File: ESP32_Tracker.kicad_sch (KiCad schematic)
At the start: 0 parts

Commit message: initial schematic started
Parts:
- added C1, C6: 0.1u, symbol Device:C
- added C2: 22u, symbol Device:C
- added C3: 1u, symbol Device:C
- added C4, C5: 10u, symbol Device:C
- added H1, H2, H3, H4: MountingHole_Pad, symbol Mechanical:MountingHole_Pad
- added J1: USB_C_Receptacle_USB2.0_16P, symbol Connector:USB_C_Receptacle_USB2.0_16P
- added R1, R2: 10k, symbol Device:R_US
- added R3, R4: 2.2k, symbol Device:R_US
- added R5, R6: 5.1k, symbol Device:R_US
- added SW1, SW2: SW_Push, symbol Switch:SW_Push
- added TP1, TP2, TP3, TP4: TestPoint, symbol Connector:TestPoint
- added U1: ESP32-S3-MINI-1, RF_Module:ESP32-S2-MINI-1, symbol RF_Module:ESP32-S3-MINI-1
- added U2: USBLC6-2SC6, Package_TO_SOT_SMD:SOT-23-6, symbol Power_Protection:USBLC6-2SC6
- added U3: XC6220B331MR-G, Package_TO_SOT_SMD:SOT-23-5, symbol Regulator_Linear:XC6220B331MR
- added U4: SAM-M10Q, RF_GPS:ublox_SAM-M8Q, symbol RF_GPS:SAM-M8Q
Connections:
- new net: J1.A5 (CC1), R5.2
- new net: J1.A6 (D+), J1.B6 (D+), U2.3 (I/O2)
- new net: J1.A7 (D-), J1.B7 (D-), U2.1 (I/O1)
- new net: J1.B5 (CC2), R6.1
- new net: R1.1, SW2.1, TP4.1, U1.4 (IO0)
- new net: C3.1, R2.1, SW1.2, TP3.1, U1.45 (EN)
- new net +3.3V: C1.1, C2.1, C5.1, C6.1, R1.2, R2.2, R3.2, R4.2, TP2.1, U1.3 (3V3), U3.5 (VOUT), U4.17 (VCC), U4.2 (VCC_IO)
- new net GND: C1.2, C2.2, C3.2, C4.1, C5.2, C6.2, J1.A1 (GND), J1.A12 (GND), J1.B1 (GND), J1.B12 (GND), J1.S1 (SHIELD), R5.1, R6.2, SW1.1, SW2.2, U1.1 (GND), U1.2 (GND), U1.42 (GND), U1.43 (GND), U1.46 (GND), U1.47 (GND), U1.48 (GND), U1.49 (GND), U1.50 (GND), U1.51 (GND), U1.52 (GND), U1.53 (GND), U1.54 (GND), U1.55 (GND), U1.56 (GND), U1.57 (GND), U1.58 (GND), U1.59 (GND), U1.60 (GND), U1.61 (GND), U1.62 (GND), U1.63 (GND), U1.64 (GND), U1.65 (GND), U2.2 (GND), U3.2 (GND), U4.1 (GND), U4.10 (GND), U4.11 (GND), U4.15 (GND), U4.16 (GND), U4.20 (GND), U4.4 (GND), U4.5 (GND), U4.6 (GND)
- new net GPS_CLK: R3.1, U1.15 (IO11), U4.12 (SCL)
- new net GPS_DATA: R4.1, U1.14 (IO10), U4.9 (SDA)
- new net USB_N: U1.23 (USB_D-), U2.6 (I/O1)
- new net USB_P: U1.24 (USB_D+), U2.4 (I/O2)
- new net VBUS: C4.2, J1.A4 (VBUS), J1.A9 (VBUS), J1.B4 (VBUS), J1.B9 (VBUS), TP1.1, U2.5 (VBUS), U3.1 (VIN), U3.3 (CE)
- no-connect marks 0 -> 8
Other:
- note added: "(4.5, 5, 5.5)V"
- note added: "5v -> 3.3v @ 1A 60mV @ 300mA"
- note added: "BOOT"
- note added: "RESET"
- note added: "Reset button? clears GNSS data and config stored in BBR"
- note added: "USB-C (DONE) LDO (DONE) GPS (IN PROGRESS) MAGNETOMETER MICROSD BATTERY MGMT."
- note added: "bypass caps typ. app."
- note added: "have primary LiPo act as backup? or add small coincell?"
- note added: "timepulse LED?"
- note added: "typ. app."
- title: (none) -> ESP32 Telemetry Tracker Board

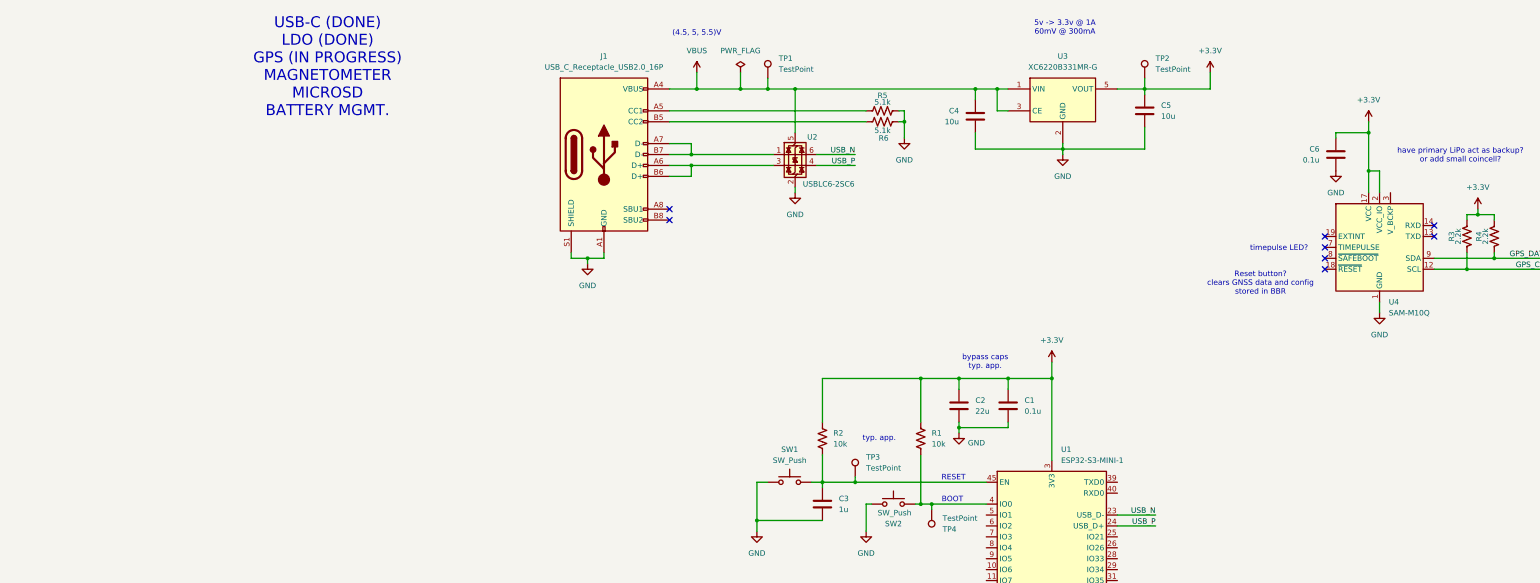
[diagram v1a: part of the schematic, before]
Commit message: magnt. symbol created
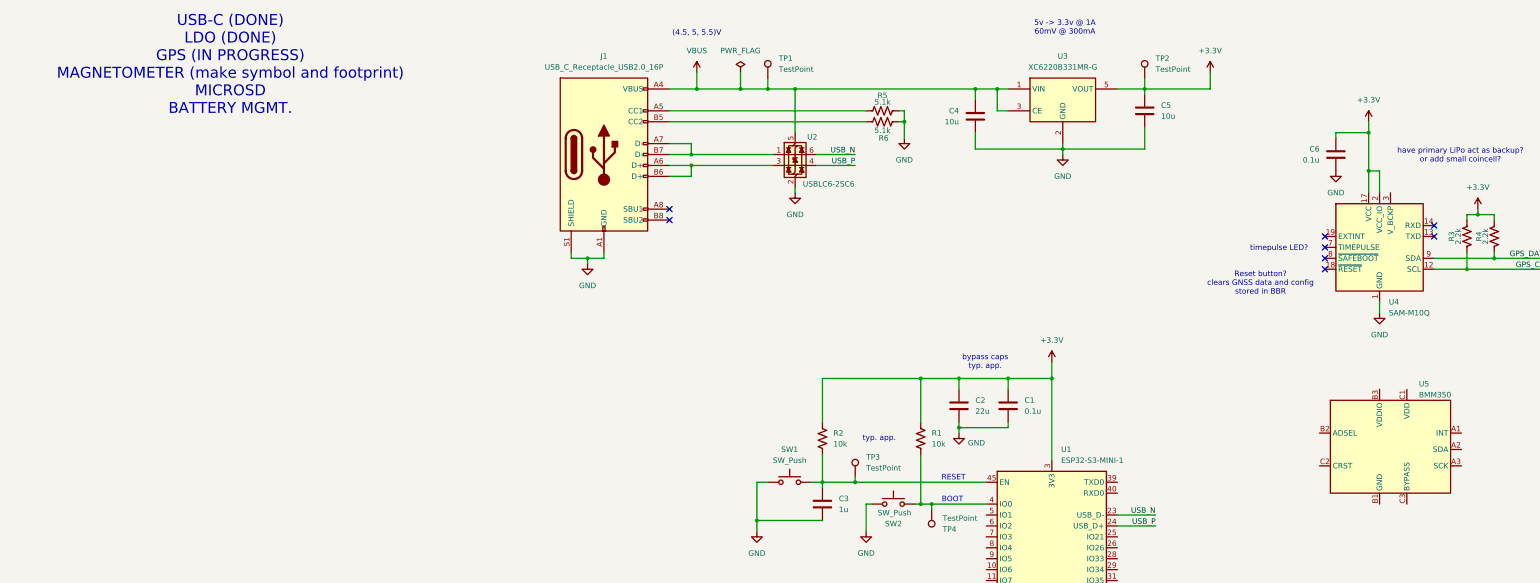
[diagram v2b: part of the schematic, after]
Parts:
- added U5: BMM350, symbol BMM350:BMM350
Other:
- note added: "USB-C (DONE) LDO (DONE) GPS (IN PROGRESS) MAGNETOMETER (make symbol and footprint) MICROSD BATTERY MGMT."
- note removed: "USB-C (DONE) LDO (DONE) GPS (IN PROGRESS) MAGNETOMETER MICROSD BATTERY MGMT."
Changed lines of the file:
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@@
 		)
 	)
-	(text "USB-C (DONE)\nLDO (DONE)\nGPS (IN PROGRESS)\nMAGNETOMETER\nMICROSD\nBATTERY MGMT."
+	(text "USB-C (DONE)\nLDO (DONE)\nGPS (IN PROGRESS)\nMAGNETOMETER (make symbol and footprint)\nMICROSD\nBATTERY MGMT."
 		(exclude_from_sim no)
-		(at -27.432 27.94 0)
+		(at -50.038 27.432 0)
 		(effects
 			(font
@@
 					(unit 1)
 				)
+			)
+		)
+	)
+	(symbol
+		(lib_id "BMM350:BMM350")
+		(at 219.71 115.57 0)
+		(unit 1)
+		(exclude_from_sim no)
+		(in_bom yes)
+		(on_board yes)
+		(dnp no)
+		(property "Reference" "U5"
+			(at 226.314 101.6 0)
+			(effects
+				(font
+					(size 1.27 1.27)
+				)
+				(justify left)
+			)
+		)
+		(property "Value" "BMM350"
+			(at 226.314 104.14 0)
+			(effects
+				(font
+					(size 1.27 1.27)
+				)
+				(justify left)
+			)
+		)
+		(property "Footprint" ""
+			(at 219.71 115.57 0)
+			(effects
+				(font
+					(size 1.27 1.27)
+				)
+				(hide yes)
+			)
+		)
+		(property "Datasheet" ""
+			(at 219.71 115.57 0)
+			(effects
+				(font
+					(size 1.27 1.27)
+				)
+				(hide yes)
+			)
+		)
+		(property "Description" ""
+			(at 219.71 115.57 0)
+			(effects
+				(font
+					(size 1.27 1.27)
+				)
+				(hide yes)
+			)
+		)
+		(pin "C1"
+		)
+		(pin "B2"
+		)
+		(pin "C2"
+		)
+		(pin "B3"
+		)
+		(pin "B1"
+		)
+		(pin "A1"
+		)
+		(pin "A2"
+		)
+		(pin "C3"
+		)
+		(pin "A3"
+		)
+		(instances
+			(project ""
+				(path "/92195c42-0bc4-473e-a890-6f85786d3c69"
+					(reference "U5")
+					(unit 1)
+				)

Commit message: new magnetometer
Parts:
- removed U5: BMM350, symbol BMM350:BMM350
- added C10, C11, C8, C9: 0.1u, symbol Device:C
- added C12: 10u, symbol Device:C
- added C13: 0.22u, symbol Device:C
- added C7: 2.2u, symbol Device:C
- added R7, R8: 10k, symbol Device:R_US
- added U5: BMM350, Package_BGA_Custom:WLCSP-9_1.28x1.28mm_P0.4mm_Bosch_BMM350, symbol Sensor_Magnetometer_Bosch:BMM350
- added U6: LIS2MDL, Package_LGA:LGA-12_2x2mm_P0.5mm, symbol Sensor_Magnetic:LIS2MDL
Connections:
- net +3.3V: now also C10.1, C11.1, C12.1, C8.1, C9.1, R7.2, R8.2, U5.B3 (VDDIO), U5.C1 (VDD), U6.10 (Vdd_IO), U6.3 (~{CS}), U6.9 (Vdd)
- net GND: now also C10.2, C11.2, C12.2, C13.2, C7.1, C8.2, C9.2, U5.B1 (GND), U5.B2 (ADSEL), U5.C3 (BYPASS), U6.6 (GND), U6.8 (GND)
- net MAG_DATA: now reaches U1.18 (IO14)
- net MAG_DATA: now also R8.1, U6.4 (SDA/SDI/SDO)
- net MAG_CLK: now reaches U1.19 (IO15)
- net MAG_CLK: now also R7.1, U6.1 (SCL/SPC)
- net MAG_INT: now reaches U1.20 (IO16)
- net MAG_INT: now also U6.7 (DRDY)
- new net: C13.1, U6.5 (C1)
- new net: C7.2, U5.C2 (CRST)
- no-connect marks 8 -> 39
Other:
- note added: "B3/C1 both need 0.1uF bypass cap TYP.APP."
- note added: "HIGH for I2C"
- note added: "LOW = 0x14 TYP.APP."
- note added: "USB-C (DONE) LDO (DONE) GPS (IN PROGRESS) MAGNETOMETER (DONE) MICROSD (TEST) BATTERY MGMT. (RESEARCH)"
- note added: "alum."
- note added: "bypass caps TYP.APP."
- note added: "ceram."
- note removed: "USB-C (DONE) LDO (DONE) GPS (IN PROGRESS) MAGNETOMETER (make symbol and footprint) MICROSD BATTERY MGMT."
- moved on the sheet: C6, H1, H2, H3, H4, R3, R4, U4

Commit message: initial schematic completed
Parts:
- removed C8, C9: 0.1u, symbol Device:C
- removed U5: BMM350, Package_BGA_Custom:WLCSP-9_1.28x1.28mm_P0.4mm_Bosch_BMM350, symbol Sensor_Magnetometer_Bosch:BMM350
- added C14, C6: 0.1u, Capacitor_SMD:C_0805_2012Metric, symbol Device:C
- added C15, C5: 10u, Capacitor_SMD:C_0805_2012Metric, symbol Device:C
- added C2: 1u, Capacitor_SMD:C_0805_2012Metric, symbol Device:C
- added C3: 2.2u, Capacitor_SMD:C_0805_2012Metric, symbol Device:C
- added J2: Conn_01x02_Socket, Connector_JST:JST_PH_S2B-PH-K_1x02_P2.00mm_Horizontal, symbol Connector:Conn_01x02_Socket
- added J3: Micro_SD_Card_Det1, symbol Connector:Micro_SD_Card_Det1
- added R12, R13, R14, R15, R16, R2, R4: 10k, Resistor_SMD:R_0805_2012Metric, symbol Device:R_US
- added R5: 100k, Resistor_SMD:R_0805_2012Metric, symbol Device:R_US
- added U3: MP2667, symbol Power_Management_MPS:MP2667
- C1: renamed from C5; footprint (none) -> Capacitor_SMD:C_0805_2012Metric; Distributor Link (none) -> https://www.lcsc.com/product-detail/C95841.html; LCSC (none) -> C95841; MPN (none) -> CL21B106KOQNNNE; Manufacturer (none) -> Samsung Electro-Mechanics
- C10, C11: footprint (none) -> Capacitor_SMD:C_0805_2012Metric; Distributor Link (none) -> https://www.lcsc.com/product-detail/C519980.html; LCSC (none) -> C519980; MPN (none) -> CC0805KRX7R7BB104; Manufacturer (none) -> YAGEO
- C12: renamed from C2; footprint (none) -> Capacitor_SMD:C_0805_2012Metric; Distributor Link (none) -> https://www.lcsc.com/product-detail/C98190.html; LCSC (none) -> C98190; MPN (none) -> CL21A226MOQNNNE; Manufacturer (none) -> Samsung Electro-Mechanics
- C13: renamed from C1; footprint (none) -> Capacitor_SMD:C_0805_2012Metric; Distributor Link (none) -> https://www.lcsc.com/product-detail/C519980.html; LCSC (none) -> C519980; MPN (none) -> CC0805KRX7R7BB104; Manufacturer (none) -> YAGEO
- C16: renamed from C3; footprint (none) -> Capacitor_SMD:C_0805_2012Metric; Distributor Link (none) -> https://www.lcsc.com/product-detail/C24123.html; LCSC (none) -> C24123; MPN (none) -> CL21B105KOFNNNE; Manufacturer (none) -> Samsung Electro-Mechanics
- C17: renamed from C13; footprint (none) -> Capacitor_SMD:C_0805_2012Metric; Distributor Link (none) -> https://www.lcsc.com/product-detail/C113853.html; LCSC (none) -> C113853; MPN (none) -> CC0805KRX7R7BB224; Manufacturer (none) -> YAGEO
- C4: footprint (none) -> Capacitor_SMD:C_0805_2012Metric; Distributor Link (none) -> https://www.lcsc.com/product-detail/C95841.html; LCSC (none) -> C95841; MPN (none) -> CL21B106KOQNNNE; Manufacturer (none) -> Samsung Electro-Mechanics
- C7: footprint (none) -> Capacitor_SMD:C_0805_2012Metric; Distributor Link (none) -> https://www.lcsc.com/product-detail/C28234.html; LCSC (none) -> C28234; MPN (none) -> CL21B225KOFNNNE; Manufacturer (none) -> Samsung Electro-Mechanics
- C8: renamed from C6; footprint (none) -> Capacitor_SMD:C_0805_2012Metric; Distributor Link (none) -> https://www.lcsc.com/product-detail/C519980.html; LCSC (none) -> C519980; MPN (none) -> CC0805KRX7R7BB104; Manufacturer (none) -> YAGEO
- C9: renamed from C12; footprint (none) -> Capacitor_SMD:C_0805_2012Metric; Distributor Link (none) -> https://www.lcsc.com/product-detail/C95841.html; LCSC (none) -> C95841; MPN (none) -> CL21B106KOQNNNE; Manufacturer (none) -> Samsung Electro-Mechanics
- H1: renamed from H2; footprint (none) -> MountingHole:MountingHole_2.2mm_M2_Pad_Via
- H2: renamed from H1; footprint (none) -> MountingHole:MountingHole_2.2mm_M2_Pad_Via
- H3, H4: footprint (none) -> MountingHole:MountingHole_2.2mm_M2_Pad_Via
- J1: footprint (none) -> Connector_USB:USB_C_Receptacle_G-Switch_GT-USB-7010ASV; Distributor Link (none) -> https://www.lcsc.com/product-detail/C2988369.html?s_z=n_GT-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; LCSC (none) -> C2988369; MPN (none) -> GT-USB-7010ASV; Manufacturer (none) -> G-Switch
- R1: renamed from R5; footprint (none) -> Resistor_SMD:R_0805_2012Metric; Distributor Link (none) -> https://www.lcsc.com/product-detail/C27834.html; LCSC (none) -> C27834; MPN (none) -> 0805W8F5101T5E; Manufacturer (none) -> UNI-ROYAL
- R10: renamed from R8; footprint (none) -> Resistor_SMD:R_0805_2012Metric; Distributor Link (none) -> https://www.lcsc.com/product-detail/C17414.html; LCSC (none) -> C17414; MPN (none) -> 0805W8F1002T5E; Manufacturer (none) -> UNI-ROYAL
- R11: renamed from R7; footprint (none) -> Resistor_SMD:R_0805_2012Metric; Distributor Link (none) -> https://www.lcsc.com/product-detail/C17414.html; LCSC (none) -> C17414; MPN (none) -> 0805W8F1002T5E; Manufacturer (none) -> UNI-ROYAL
- R3: renamed from R6; footprint (none) -> Resistor_SMD:R_0805_2012Metric; Distributor Link (none) -> https://www.lcsc.com/product-detail/C27834.html; LCSC (none) -> C27834; MPN (none) -> 0805W8F5101T5E; Manufacturer (none) -> UNI-ROYAL
- R6: renamed from R3; footprint (none) -> Resistor_SMD:R_0805_2012Metric; Distributor Link (none) -> https://www.lcsc.com/product-detail/C17520.html; LCSC (none) -> C17520; MPN (none) -> 0805W8F2201T5E; Manufacturer (none) -> UNI-ROYAL
- R7: renamed from R4; footprint (none) -> Resistor_SMD:R_0805_2012Metric; Distributor Link (none) -> https://www.lcsc.com/product-detail/C17520.html; LCSC (none) -> C17520; MPN (none) -> 0805W8F2201T5E; Manufacturer (none) -> UNI-ROYAL
- R8: renamed from R2; footprint (none) -> Resistor_SMD:R_0805_2012Metric; Distributor Link (none) -> https://www.lcsc.com/product-detail/C17414.html; LCSC (none) -> C17414; MPN (none) -> 0805W8F1002T5E; Manufacturer (none) -> UNI-ROYAL
- R9: renamed from R1; footprint (none) -> Resistor_SMD:R_0805_2012Metric; Distributor Link (none) -> https://www.lcsc.com/product-detail/C17414.html; LCSC (none) -> C17414; MPN (none) -> 0805W8F1002T5E; Manufacturer (none) -> UNI-ROYAL
- SW1, SW2: footprint (none) -> Button_Switch_SMD:SW_SPST_TS-1088-xR020; Distributor Link (none) -> https://www.lcsc.com/product-detail/C720477.html?s_z=n_push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; LCSC (none) -> C720477; MPN (none) -> TS-1088-AR02016; Manufacturer (none) -> XUNPU
- TP1, TP2, TP3, TP4: footprint (none) -> TestPoint:TestPoint_Pad_D1.5mm
- U1: renamed from U3; Distributor Link (none) -> https://www.lcsc.com/product-detail/C86534.html?s_z=n_xc622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; LCSC (none) -> C86534; MPN (none) -> XC6220B331MR-G; Manufacturer (none) -> TOREX
- U2: Distributor Link (none) -> https://www.lcsc.com/product-detail/C2827654.html?s_z=n_USB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; LCSC (none) -> C2827654; MPN (none) -> USBLC6-2SC6; Manufacturer (none) -> TECH PUBLIC
- U4: Distributor Link (none) -> https://www.digikey.com/en/products/detail/u-blox/SAM-M10Q-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
- U5: renamed from U6; Distributor Link (none) -> https://www.digikey.com/en/products/detail/stmicroelectroni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
- U6: renamed from U1; Distributor Link (none) -> https://www.lcsc.com/product-detail/C2913206.html?s_z=n_esp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; LCSC (none) -> C2913206; MPN (none) -> ESP32-S3-MINI-1-N8; Manufacturer (none) -> ESPRESSIF
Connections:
- net +3.3V: now also C7.1, U4.3 (V_BCKP), C14.1, C15.1, J3.4 (VDD), R12.2, R13.2, R14.2, R15.2, R16.2, R5.1
- net GND: now also C7.2, H1.1, H2.1, H3.1, H4.1, C14.2, C15.2, C2.1, C3.2, C5.1, C6.2, J2.1 (Pin_1), J3.10 (SHIELD), J3.6 (VSS), R4.2, U3.5 (GND); no longer C7.1
- net GPS_CLK: now also U6.10 (IO6); no longer U6.15 (IO11)
- net GPS_DATA: now also U6.9 (IO5); no longer U6.14 (IO10)
- net VBUS: now also C2.2, R2.2, U3.1 (IN); no longer C4.2, U1.1 (VIN), U1.3 (CE)
- net SD_DETECT: now reaches U6.13 (IO9)
- net SD_DETECT: now also J3.9 (DET), R16.1
- net SD_CLK: now reaches U6.16 (IO12)
- net SD_CLK: now also J3.5 (CLK), R14.1
- net SD_MISO: now reaches U6.17 (IO13)
- net SD_MISO: now also J3.7 (DAT0), R15.1
- net BATT_DATA: now reaches U6.29 (IO34)
- net BATT_DATA: now also U3.7 (SDA)
- net BATT_CLK: now reaches U6.31 (IO35)
- net BATT_CLK: now also U3.6 (SCL)
- new net: R2.1, R4.1, U3.2 (NTC)
- new net: C5.2, J2.2 (Pin_2), U3.8 (BATT), U3.9 (BATT)
- new net: C6.1, U3.4 (VDD)
- new net: C3.1, C4.2, U1.1 (VIN), U1.3 (CE), U3.10 (SYS)
- new net INT: R5.2, U3.3 (INT)
- new net SD_CS: J3.2 (DAT3/CD), R12.1, U6.14 (IO10)
- new net SD_MOSI: J3.3 (CMD), R13.1, U6.15 (IO11)
- no-connect marks 39 -> 34
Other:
- note added: "3.7V 2Ah LiPo"
- note added: "Batt IC Alternatives: MP2667 MCP73871"
- note added: "Charging IC + PWR Path Programmable charge current"
- note added: "POLARITY OF JST?"
- note added: "USB-C (DONE) LDO (DONE) GPS (DONE) MAGNETOMETER (DONE) MICROSD (DONE) BATTERY MGMT. (DONE) BUTTONS (IN PROGRESS) STATUS LEDs (IN PROGRESS)"
- note added: "Why LiPo? Thin, compact Adafruit protection circuitry right voltage not great lifespan compared to others"
- note added: "adafruit LiPo has built in protection circuitry only need charging IC"
- note added: "sys load"
- note removed: "B3/C1 both need 0.1uF bypass cap TYP.APP."
- note removed: "LOW = 0x14 TYP.APP."
- note removed: "USB-C (DONE) LDO (DONE) GPS (IN PROGRESS) MAGNETOMETER (DONE) MICROSD (TEST) BATTERY MGMT. (RESEARCH)"
- moved on the sheet: C1, C10, C11, C12, C13, C16, C17, C4, C8, C9, H1, H2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

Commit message: MP Footprint created
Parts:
- added C18: 0.1u, Capacitor_SMD:C_0805_2012Metric, symbol Device:C
- added D1: LED, symbol Device:LED
- added R17: 2.2k, Resistor_SMD:R_0805_2012Metric, symbol Device:R_US
- added R18: 10k, Resistor_SMD:R_0805_2012Metric, symbol Device:R_US
- added SW3: SW_Push, Button_Switch_SMD:SW_SPST_TS-1088-xR020, symbol Switch:SW_Push
- added TP5, TP6, TP7, TP8: TestPoint, TestPoint:TestPoint_Pad_D1.5mm, symbol Connector:TestPoint
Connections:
- net +3.3V: now also R18.2
- net GND: now also C18.2, D1.1 (K), SW3.2
- net at J1.A6 (D+), J1.B6 (D+), U2.3 (I/O2): now also TP6.1
- net at J1.A7 (D-), J1.B7 (D-), U2.1 (I/O1): now also TP5.1
- net at C5.2, J2.2 (Pin_2), U3.8 (BATT)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: now also TP7.1
- net at C3.1, C4.2, U1.1 (VIN)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: now also TP8.1
- net at U6.25 (IO21): now also C18.1, R18.1, SW3.1
- net at U6.38 (IO42): now also R17.2
- new net: D1.2 (A), R17.1
- no-connect marks 34 -> 32
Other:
- note added: "USB-C (DONE) LDO (DONE) GPS (DONE) MAGNETOMETER (DONE) MICROSD (DONE) BATTERY MGMT. (DONE) BUTTONS (IN PROGRESS) STATUS LEDs (IN PROGRESS) RTC for Low PWR mode (Shipping mode on MP2667?)"
- note added: "logging on/off"
- note added: "status LED"
- note removed: "USB-C (DONE) LDO (DONE) GPS (DONE) MAGNETOMETER (DONE) MICROSD (DONE) BATTERY MGMT. (DONE) BUTTONS (IN PROGRESS) STATUS LEDs (IN PROGRESS)"
- company: (none) -> ECE-212 Team 7
- moved on the sheet: C10, C11, C17, C7, C8, C9, H1, H2, H3, H4, R10, R11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

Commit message: models added
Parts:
- D1: footprint (none) -> LED_SMD:LED_0805_2012Metric; Distributor Link (none) -> https://www.lcsc.com/product-detail/C965812.html; LCSC (none) -> C965812; MPN (none) -> XL-2012SURC; Manufacturer (none) -> XINGLIGHT
- J3: footprint (none) -> MSD-4-A_DL:CUI_MSD-4-A; Distributor Link (none) -> https://www.digikey.com/en/products/detail/same-sky-formerl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; MPN (none) -> MSD-4-A; Manufacturer (none) -> Same Sky (Formerly CUI Devices)
- U3: footprint (none) -> MP2667_DL:QFN-10_2MMx2MM_MNP; Distributor Link (none) -> https://www.digikey.com/en/products/detail/monolithic-power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; MPN (none) -> MP2667GG-0000-Z; Manufacturer (none) -> Monolithic Power Systems Inc.
- U4: MPN (none) -> SAM-M10Q-00B; Manufacturer (none) -> u-blox
- U5: MPN (none) -> LIS2MDLTR; Manufacturer (none) -> STMicroelectronics
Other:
- note added: "USB-C (DONE) LDO (DONE) GPS (DONE) MAGNETOMETER (DONE) MICROSD (DONE) BATTERY MGMT. (DONE) BUTTONS (IN PROGRESS) STATUS LEDs (IN PROGRESS) OLED CONN (?) RTC for Low PWR mode (Shipping mode on MP2667?)"
- note removed: "USB-C (DONE) LDO (DONE) GPS (DONE) MAGNETOMETER (DONE) MICROSD (DONE) BATTERY MGMT. (DONE) BUTTONS (IN PROGRESS) STATUS LEDs (IN PROGRESS) RTC for Low PWR mode (Shipping mode on MP2667?)"
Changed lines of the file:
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@@
 		)
 	)
-	(text "USB-C (DONE)\nLDO (DONE)\nGPS (DONE)\nMAGNETOMETER (DONE)\nMICROSD (DONE)\nBATTERY MGMT. (DONE)\nBUTTONS (IN PROGRESS)\nSTATUS LEDs (IN PROGRESS)\nRTC for Low PWR mode (Shipping mode on MP2667?)"
+	(text "USB-C (DONE)\nLDO (DONE)\nGPS (DONE)\nMAGNETOMETER (DONE)\nMICROSD (DONE)\nBATTERY MGMT. (DONE)\nBUTTONS (IN PROGRESS)\nSTATUS LEDs (IN PROGRESS)\nOLED CONN (?)\nRTC for Low PWR mode (Shipping mode on MP2667?)"
 		(exclude_from_sim no)
 		(at -55.372 29.718 0)
@@
 			)
 		)
-		(property "MPN" ""
+		(property "MPN" "LIS2MDLTR"
 			(at 204.47 139.7 0)
 			(effects
@@
 			)
 		)
-		(property "Manufacturer" ""
+		(property "Manufacturer" "STMicroelectronics"
 			(at 204.47 139.7 0)
 			(effects
@@
 			)
 		)
-		(property "Footprint" ""
+		(property "Footprint" "MP2667_DL:QFN-10_2MMx2MM_MNP"
 			(at 148.59 43.18 0)
 			(effects
@@
 			)
 		)
+		(property "Distributor Link" "https://www.digikey.com/en/products/detail/monolithic-power-systems-inc/MP2667GG-0000-Z/11611000"
+			(at 148.59 43.18 0)
+			(effects
+				(font
+					(size 1.27 1.27)
+				)
+				(hide yes)
+			)
+		)
+		(property "MPN" "MP2667GG-0000-Z"
+			(at 148.59 43.18 0)
+			(effects
+				(font
+					(size 1.27 1.27)
+				)
+				(hide yes)
+			)
+		)
+		(property "Manufacturer" "Monolithic Power Systems Inc."
+			(at 148.59 43.18 0)
+			(effects
+				(font
+					(size 1.27 1.27)
+				)
+				(hide yes)
+			)
+		)
 		(pin "10"
 		)
@@
 			)
 		)
-		(property "MPN" ""
+		(property "MPN" "SAM-M10Q-00B"
 			(at 240.03 87.63 0)
 			(effects
@@
 			)
 		)
-		(property "Manufacturer" ""
+		(property "Manufacturer" "u-blox"
 			(at 240.03 87.63 0)
 			(effects
@@
 			)
 		)
-		(property "Footprint" ""
+		(property "Footprint" "MSD-4-A_DL:CUI_MSD-4-A"
 			(at 443.23 128.27 0)
 			(effects
@@
 			)
 		)
-		(property "MPN" ""
+		(property "MPN" "MSD-4-A"
 			(at 391.16 146.05 0)
 			(effects
@@
 			)
 		)
-		(property "Manufacturer" ""
+		(property "Manufacturer" "Same Sky (Formerly CUI Devices)"
+			(at 391.16 146.05 0)
+			(effects
+				(font
+					(size 1.27 1.27)
+				)
+				(hide yes)
+			)
+		)
+		(property "Distributor Link" "https://www.digikey.com/en/products/detail/same-sky-formerly-cui-devices/MSD-4-A/21796808"
 			(at 391.16 146.05 0)
 			(effects
@@
 			)
 		)
-		(property "Footprint" ""
+		(property "Footprint" "LED_SMD:LED_0805_2012Metric"
 			(at 118.11 170.18 0)
 			(effects
@@
 			)
 		)
-		(property "Datasheet" "~"
+		(property "Datasheet" "https://www.lcsc.com/datasheet/C965812.pdf"
 			(at 118.11 170.18 0)
 			(effects
@@
 			(at 118.11 170.18 0)
 			(effects
+				(font
+					(size 1.27 1.27)
+				)
+				(hide yes)
+			)
+		)
+		(property "Distributor Link" "https://www.lcsc.com/product-detail/C965812.html"
+			(at 118.11 170.18 0)
+			(effects
+				(font
+					(size 1.27 1.27)
+				)
+				(hide yes)
+			)
+		)
+		(property "LCSC" "C965812"
+			(at 118.11 170.18 0)
+			(effects
+				(font
+					(size 1.27 1.27)
+				)
+				(hide yes)
+			)
+		)
+		(property "MPN" "XL-2012SURC"
+			(at 118.11 170.18 0)
+			(effects
+				(font
+					(size 1.27 1.27)
+				)
+				(hide yes)
+			)
+		)
+		(property "Manufacturer" "XINGLIGHT"
+			(at 118.11 170.18 0)
+			(effects

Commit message: notes
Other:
- note added: "USB-C (DONE) LDO (DONE) GPS (DONE) MAGNETOMETER (DONE) MICROSD (DONE) BATTERY MGMT. (DONE) BUTTONS (IN PROGRESS) STATUS LEDs (IN PROGRESS) PWR CONSUMPTION (IN PROGRESS) OLED CONN (?) RTC for Low PWR mode (Shipping mode on MP2667?)"
- note added: "toggle button record button low power"
- note removed: "USB-C (DONE) LDO (DONE) GPS (DONE) MAGNETOMETER (DONE) MICROSD (DONE) BATTERY MGMT. (DONE) BUTTONS (IN PROGRESS) STATUS LEDs (IN PROGRESS) OLED CONN (?) RTC for Low PWR mode (Shipping mode on MP2667?)"
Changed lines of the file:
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@@
 		)
 	)
-	(text "USB-C (DONE)\nLDO (DONE)\nGPS (DONE)\nMAGNETOMETER (DONE)\nMICROSD (DONE)\nBATTERY MGMT. (DONE)\nBUTTONS (IN PROGRESS)\nSTATUS LEDs (IN PROGRESS)\nOLED CONN (?)\nRTC for Low PWR mode (Shipping mode on MP2667?)"
+	(text "USB-C (DONE)\nLDO (DONE)\nGPS (DONE)\nMAGNETOMETER (DONE)\nMICROSD (DONE)\nBATTERY MGMT. (DONE)\n\n\nBUTTONS (IN PROGRESS)\nSTATUS LEDs (IN PROGRESS)\nPWR CONSUMPTION (IN PROGRESS)\nOLED CONN (?)\nRTC for Low PWR mode (Shipping mode on MP2667?)"
 		(exclude_from_sim no)
 		(at -55.372 29.718 0)
@@
 		(effects
 			(font
+				(size 1.27 1.27)
+			)
+		)
+	)
+	(text "toggle button\nrecord button\nlow power"
+		(exclude_from_sim no)
+		(at -20.32 167.64 0)
+		(effects
+			(font
